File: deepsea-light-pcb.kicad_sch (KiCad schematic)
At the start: 6 parts, among them CN1 XT60PW-M, U1 Pico, U2 2604-1106, U3 2604-1106, U4 2604-1106, U5 2604-1106

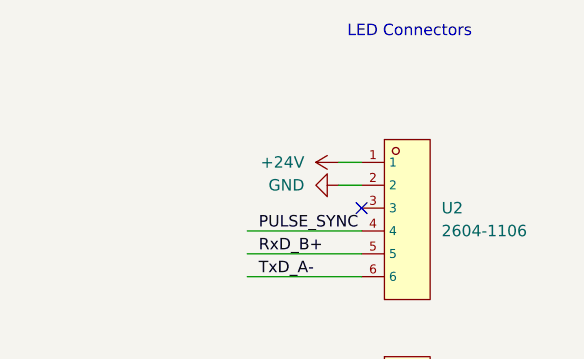
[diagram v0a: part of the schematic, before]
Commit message: Add note on wire gauge
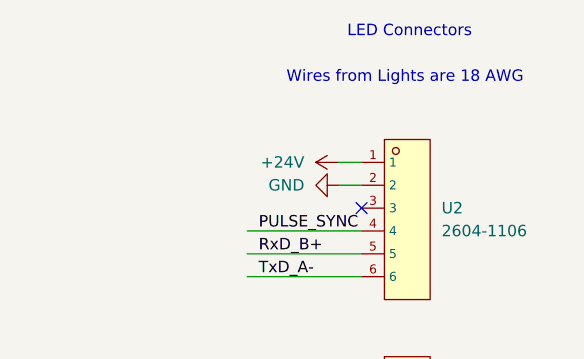
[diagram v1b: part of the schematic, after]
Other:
- note added: "Wires from Lights are 18 AWG"
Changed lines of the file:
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@@
+		)
+	)
+	(text "Wires from Lights are 18 AWG"
+		(exclude_from_sim no)
+		(at 205.486 43.942 0)
+		(effects
+			(font
+				(size 1.27 1.27)
+			)
 		)
 	)

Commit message: update
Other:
- note added: "Power is ~ 100 watts at 24 volts, so need to support just over 4 amps"
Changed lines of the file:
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@@
+		)
+	)
+	(text "Power is ~ 100 watts at 24 volts, so need to support just over 4 amps"
+		(exclude_from_sim no)
+		(at 203.708 46.736 0)
+		(effects
+			(font
+				(size 1.27 1.27)
+			)
 		)
 	)
 	(text "Wires from Lights are 18 AWG"
 		(exclude_from_sim no)
-		(at 205.486 43.942 0)
+		(at 205.232 42.672 0)
 		(effects
 			(font

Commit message: Updates
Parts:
- added U6: SparkFun_BabyBuck_5V, Deepsea_light_lib:SparkFun_BabyBuck_5V, symbol Deepsea_light_lib:SparkFun_BabyBuck_5V
- added U7: SparkFun_RS485_Breakout, Deepsea_light_lib:SparkFun_RS485_Breakout, symbol Deepsea_light_lib:SparkFun_RS485_Breakout
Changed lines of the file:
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@@
+	)
+	(symbol
+		(lib_id "Deepsea_light_lib:SparkFun_RS485_Breakout")
+		(at 63.5 45.72 0)
+		(unit 1)
+		(body_style 1)
+		(exclude_from_sim no)
+		(in_bom yes)
+		(on_board yes)
+		(in_pos_files yes)
+		(dnp no)
+		(fields_autoplaced yes)
+		(property "Reference" "U7"
+			(at 63.5 30.48 0)
+			(show_name no)
+			(do_not_autoplace no)
+			(effects
+				(font
+					(size 1.27 1.27)
+				)
+			)
+		)
+		(property "Value" "SparkFun_RS485_Breakout"
+			(at 63.5 33.02 0)
+			(show_name no)
+			(do_not_autoplace no)
+			(effects
+				(font
+					(size 1.27 1.27)
+				)
+			)
+		)
+		(property "Footprint" "Deepsea_light_lib:SparkFun_RS485_Breakout"
+			(at 63.5 59.69 0)
+			(hide yes)
+			(show_name no)
+			(do_not_autoplace no)
+			(effects
+				(font
+					(size 1.27 1.27)
+					(italic yes)
+				)
+			)
+		)
+		(property "Datasheet" "https://github.com/sparkfun/RS-485_Breakout"
+			(at 63.5 45.72 0)
+			(hide yes)
+			(show_name no)
+			(do_not_autoplace no)
+			(effects
+				(font
+					(size 1.27 1.27)
+				)
+				(justify left)
+			)
+		)
+		(property "Description" "SparkFun Transceiver Breakout RS-485 (SP3485), 3.3V half-duplex, RTS drives DE/RE, used as a solder-down module"
+			(at 63.5 45.72 0)
+			(hide yes)
+			(show_name no)
+			(do_not_autoplace no)
+			(effects
+				(font
+					(size 1.27 1.27)
+				)
+			)
+		)
+		(pin "1"
+		)
+		(pin "7"
+		)
+		(pin "6"
+		)
+		(pin "5"
+		)
+		(pin "3"
+		)
+		(pin "4"
+		)
+		(pin "2"
+		)
+		(pin "8"
+		)
+		(instances
+			(project "deepsea-light-pcb"
+				(path "/99abfaa1-ae0d-4c93-9def-8bea19834d01"
+					(reference "U7")
+					(unit 1)
+				)
+			)
+		)
 	)
 	(symbol
@@
 					(unit 1)
 				)
+			)
+		)
+	)
+	(symbol
+		(lib_id "Deepsea_light_lib:SparkFun_BabyBuck_5V")
+		(at 64.77 143.51 0)
+		(unit 1)
+		(body_style 1)
+		(exclude_from_sim no)
+		(in_bom yes)
+		(on_board yes)
+		(in_pos_files yes)
+		(dnp no)
+		(fields_autoplaced yes)
+		(property "Reference" "U6"
+			(at 64.77 133.35 0)
+			(show_name no)
+			(do_not_autoplace no)
+			(effects
+				(font
+					(size 1.27 1.27)
+				)
+			)
+		)
+		(property "Value" "SparkFun_BabyBuck_5V"
+			(at 64.77 135.89 0)
+			(show_name no)
+			(do_not_autoplace no)
+			(effects
+				(font
+					(size 1.27 1.27)
+				)
+			)
+		)
+		(property "Footprint" "Deepsea_light_lib:SparkFun_BabyBuck_5V"
+			(at 64.77 154.94 0)
+			(hide yes)
+			(show_name no)
+			(do_not_autoplace no)
+			(effects
+				(font
+					(size 1.27 1.27)
+					(italic yes)
+				)
+			)
+		)
+		(property "Datasheet" "https://docs.sparkfun.com/SparkFun_Buck_Regulator_AP63357DV-7/"
+			(at 64.77 143.51 0)
+			(hide yes)
+			(show_name no)
+			(do_not_autoplace no)
+			(effects
+				(font
+					(size 1.27 1.27)
+				)
+				(justify left)
+			)
+		)
+		(property "Description" "SparkFun BabyBuck Regulator Breakout 5V (AP63357), 3.8-32V in, 5V/3.5A out, used as a solder-down module"
+			(at 64.77 143.51 0)
+			(hide yes)
+			(show_name no)
+			(do_not_autoplace no)
+			(effects
+				(font
+					(size 1.27 1.27)
+				)
+			)
+		)
+		(pin "1"
+		)
+		(pin "4"
+		)
+		(pin "2"
+		)
+		(pin "3"
+		)
+		(instances
+			(project "deepsea-light-pcb"
+				(path "/99abfaa1-ae0d-4c93-9def-8bea19834d01"
+					(reference "U6")
+					(unit 1)
+				)

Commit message: Update
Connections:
- net +24V: now also U6.2 (VIN)
- net GND: now also U1.13 (GND), U1.18 (GND), U1.23 (GND), U1.28 (GND), U1.3 (GND), U1.38 (GND), U1.8 (GND), U6.3 (GND), U7.5 (GND)
- net +5V: now reaches U1.40 (VBUS)
- net +5V: now also U6.4 (VOUT)

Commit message: updates
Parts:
- removed U6: SparkFun_BabyBuck_5V, Deepsea_light_lib:SparkFun_BabyBuck_5V, symbol Deepsea_light_lib:SparkFun_BabyBuck_5V
- added U6: 2604-1103, Deepsea_light_lib:CONN-TH_2604-1103, symbol Deepsea_light_lib:2604-1103
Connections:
- net +5V: now also U1.39 (VSYS), U7.1 (3-5V), U6.1; no longer U1.40 (VBUS)
- net GND: now also U6.3; no longer CN1.1 (-), U2.2, U3.2, U4.2, U5.2
- net LIGHT_GND: now reaches CN1.3
- net LIGHT_GND: now also CN1.1 (-), CN1.4, U2.2, U3.2, U4.2, U5.2
- net LIGHTS_RX: now reaches U7.2 (RX-I)
- net LIGHTS_RX: now also U1.2 (GPIO1)
- net LIGHTS_TX: now reaches U7.3 (TX-O)
- net LIGHTS_TX: now also U1.1 (GPIO0)
- net LIGHTS_RTS: now reaches U7.4 (RTS)
- net LIGHTS_RTS: now also U1.25 (GPIO19)
- net PWM_INPUT: now reaches U1.21 (GPIO16)
- net PWM_INPUT: now also U6.2
- no-connect marks 4 -> 24
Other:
- note added: "Navigator Input"
- moved on the sheet: CN1, U1, U2, U3, U4, U5, U7

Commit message: Add callouts for all components
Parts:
- CN1: Callout (none) -> Input 24 V
- U1: Callout (none) -> Raspberry Pi Pico 2
- U2: Callout (none) -> Light 1 Connector
- U3: Callout (none) -> Light 2 Connector
- U4: Callout (none) -> Light 3 Connector
- U5: Callout (none) -> Light 4 Connector
- U6: Callout (none) -> PWM Input
- U7: Callout (none) -> RS-485 Transceiver
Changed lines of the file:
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@@
+			)
+		)
+		(property "Callout" "Light 1 Connector"
+			(at 170.18 54.61 0)
+			(hide yes)
+			(show_name no)
+			(do_not_autoplace no)
+			(effects
+				(font
+					(size 1.27 1.27)
+				)
 			)
 		)
@@
 			)
 		)
+		(property "Callout" "Light 4 Connector"
+			(at 170.18 130.81 0)
+			(hide yes)
+			(show_name no)
+			(do_not_autoplace no)
+			(effects
+				(font
+					(size 1.27 1.27)
+				)
+			)
+		)
 		(pin "4"
 		)
@@
 			)
 		)
+		(property "Callout" "Light 2 Connector"
+			(at 170.18 78.74 0)
+			(hide yes)
+			(show_name no)
+			(do_not_autoplace no)
+			(effects
+				(font
+					(size 1.27 1.27)
+				)
+			)
+		)
 		(pin "4"
 		)
@@
 			)
 		)
+		(property "Callout" "Input 24 V"
+			(at 229.87 57.15 0)
+			(hide yes)
+			(show_name no)
+			(do_not_autoplace no)
+			(effects
+				(font
+					(size 1.27 1.27)
+				)
+			)
+		)
 		(pin "1"
 		)
@@
 			)
 		)
+		(property "Callout" "RS-485 Transceiver"
+			(at 74.93 53.34 0)
+			(hide yes)
+			(show_name no)
+			(do_not_autoplace no)
+			(effects
+				(font
+					(size 1.27 1.27)
+				)
+			)
+		)
 		(pin "1"
 		)
@@
 			)
 		)
+		(property "Callout" "Raspberry Pi Pico 2"
+			(at 76.2 134.62 0)
+			(hide yes)
+			(show_name no)
+			(do_not_autoplace no)
+			(effects
+				(font
+					(size 1.27 1.27)
+				)
+			)
+		)
 		(pin "38"
 		)
@@
 			)
 		)
+		(property "Callout" "PWM Input"
+			(at 229.87 87.63 0)
+			(hide yes)
+			(show_name no)
+			(do_not_autoplace no)
+			(effects
+				(font
+					(size 1.27 1.27)
+				)
+			)
+		)
 		(pin "2"
 		)
@@
 			(at 170.18 104.14 0)
 			(hide yes)
+			(show_name no)
+			(do_not_autoplace no)
+			(effects
+				(font
+					(size 1.27 1.27)
+				)
+			)
+		)
+		(property "Callout" "Light 3 Connector"
+			(at 170.18 104.14 0)
+			(hide yes)

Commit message: Update deepsea-light-pcb.kicad_sch
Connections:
- net RxD_B+: now also U7.7 (A)
- net TxD_A-: now also U7.8 (B)
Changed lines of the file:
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@@
+		)
+	)
+	(label "RxD_B+"
+		(at 88.9 50.8 0)
+		(effects
+			(font
+				(size 1.27 1.27)
+			)
+			(justify left bottom)
 		)
 	)
@@
 		(effects
 			(font
+				(size 1.27 1.27)
+			)
+			(justify left bottom)
+		)
+	)
+	(label "TxD_A-"
+		(at 88.9 53.34 0)
+		(effects
+			(font

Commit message: Routing progress
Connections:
- removed net PULSE_SYNC: U2.4, U3.4, U4.4, U5.4
- no-connect marks 24 -> 28
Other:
- note added: "Pulse Sync Pin"
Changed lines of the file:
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@@
+		)
+	)
+	(text "Pulse Sync Pin"
+		(exclude_from_sim no)
+		(at 144.78 105.41 0)
+		(effects
+			(font
+				(size 1.27 1.27)
+			)
 		)
 	)
@@
 		)
 	)
+	(text "Pulse Sync Pin"
+		(exclude_from_sim no)
+		(at 144.526 80.264 0)
+		(effects
+			(font
+				(size 1.27 1.27)
+			)
+		)
+	)
+	(text "Pulse Sync Pin"
+		(exclude_from_sim no)
+		(at 143.51 55.88 0)
+		(effects
+			(font
+				(size 1.27 1.27)
+			)
+		)
+	)
 	(text "Wires from Lights are 18 AWG"
 		(exclude_from_sim no)
 		(at 170.942 37.592 0)
+		(effects
+			(font
+				(size 1.27 1.27)
+			)
+		)
+	)
+	(text "Pulse Sync Pin"
+		(exclude_from_sim no)
+		(at 144.526 132.334 0)
 		(effects
 			(font
@@
 	)
 	(no_connect
+		(at 153.67 132.08)
+	)
+	(no_connect
 		(at 58.42 123.19)
 	)
@@
 	)
 	(no_connect
+		(at 153.67 105.41)
+	)
+	(no_connect
 		(at 93.98 138.43)
 	)
@@
 	)
 	(no_connect
+		(at 153.67 55.88)
+	)
+	(no_connect
 		(at 93.98 143.51)
 	)
@@
 	(no_connect
 		(at 166.37 102.87)
+	)
+	(no_connect
+		(at 153.67 80.01)
 	)
 	(wire
@@
 		)
 	)
-	(label "PULSE_SYNC"
-		(at 154.94 55.88 0)
-		(effects
-			(font
-				(size 1.27 1.27)
-			)
-			(justify left bottom)
-		)
-	)
 	(label "RxD_B+"
 		(at 154.94 58.42 0)
@@
 		)
 	)
-	(label "PULSE_SYNC"
-		(at 154.94 132.08 0)
-		(effects
-			(font
-				(size 1.27 1.27)
-			)
-			(justify left bottom)
-		)
-	)
 	(label "TxD_A-"
 		(at 88.9 53.34 0)
@@
 		)
 	)
-	(label "PULSE_SYNC"
-		(at 154.94 80.01 0)
-		(effects
-			(font
-				(size 1.27 1.27)
-			)
-			(justify left bottom)
-		)
-	)
 	(label "TxD_A-"
 		(at 154.94 110.49 0)
@@
 		(effects
 			(font
-				(size 1.27 1.27)
-			)
-			(justify left bottom)
-		)
-	)
-	(label "PULSE_SYNC"
-		(at 154.94 105.41 0)
-		(effects
-			(font
